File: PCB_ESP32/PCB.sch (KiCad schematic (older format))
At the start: 26 parts, among them J3 I2C, J4 I2C, J5 WindVane, J6 WindSpeed, J7 ATTINY24, J7 Rain, J8 ReedSwitches-WindVane, U1 MCP1702-5002E_TO92 5V, U2 MCP1700-3302E_TO92 3.3V, U5 ATtiny24A-PU WindDir

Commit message: PCB for ESP32
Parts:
- removed C12: 100nF, symbol Device:C_Small
- removed J7: ATTINY24, symbol Connector_Generic:Conn_01x04
- removed J8: ReedSwitches-WindVane, symbol Connector_Generic:Conn_02x05_Odd_Even
- removed U5: ATtiny24A-PU WindDir, Package_DIP:DIP-14_W7.62mm, symbol MCU_Microchip_ATtiny:ATtiny24A-PU
- added C8, C9: 0.1uF, Capacitor_THT:CP_Radial_Tantal_D4.5mm_P5.00mm, symbol Device:C
- added R5: 20M, Resistor_THT:R_Axial_DIN0207_L6.3mm_D2.5mm_P10.16mm_Horizontal, symbol Device:R
- added R6, R8: 10M, Resistor_THT:R_Axial_DIN0207_L6.3mm_D2.5mm_P10.16mm_Horizontal, symbol Device:R
- added R7: 5M2, Resistor_THT:R_Axial_DIN0207_L6.3mm_D2.5mm_P10.16mm_Horizontal, symbol Device:R
- C1: footprint (none) -> Capacitor_THT:CP_Radial_D8.0mm_P5.00mm
- C2: renamed from C10; footprint (none) -> Capacitor_THT:CP_Radial_Tantal_D4.5mm_P5.00mm
- C3: renamed from C9; footprint (none) -> Capacitor_THT:CP_Radial_Tantal_D4.5mm_P5.00mm
- C4: renamed from C2; footprint (none) -> Capacitor_THT:CP_Radial_D8.0mm_P5.00mm
- C5: renamed from C3; footprint (none) -> Capacitor_THT:CP_Radial_D8.0mm_P5.00mm
- C6: renamed from C7; footprint (none) -> Capacitor_THT:CP_Radial_Tantal_D4.5mm_P5.00mm
- C7: renamed from C8; footprint (none) -> Capacitor_THT:CP_Radial_Tantal_D4.5mm_P5.00mm
- D1: footprint (none) -> Diode_THT:D_DO-41_SOD81_P10.16mm_Horizontal
- GND1, GND2: footprint (none) -> Connector_JST:JST_XH_B2B-XH-AM_1x02_P2.50mm_Vertical
- J3, J4: footprint (none) -> Connector_JST:JST_XH_B4B-XH-A_1x04_P2.50mm_Vertical
- J5: footprint (none) -> Connector_PinHeader_2.54mm:PinHeader_2x05_P2.54mm_Vertical
- J6, J7: footprint (none) -> Connector_JST:JST_XH_B3B-XH-A_1x03_P2.50mm_Vertical
- R1, R2, R3, R4: footprint (none) -> Resistor_THT:R_Axial_DIN0207_L6.3mm_D2.5mm_P10.16mm_Horizontal
- U3: renamed from U?; footprint RF_Module:ESP32-WROOM-32 -> PCB_ESP32:ESP32DevKit
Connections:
- net GND: now also C8.1, C9.1, R6.2, R8.2
- net at C1.1, C2.2, GND1.2 (Pin_2)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: now also R5.1
- net at U3.6 (IO34): now also C8.2, R5.2, R6.1
- net at U3.7 (IO35): now also C9.2, R7.2, R8.1

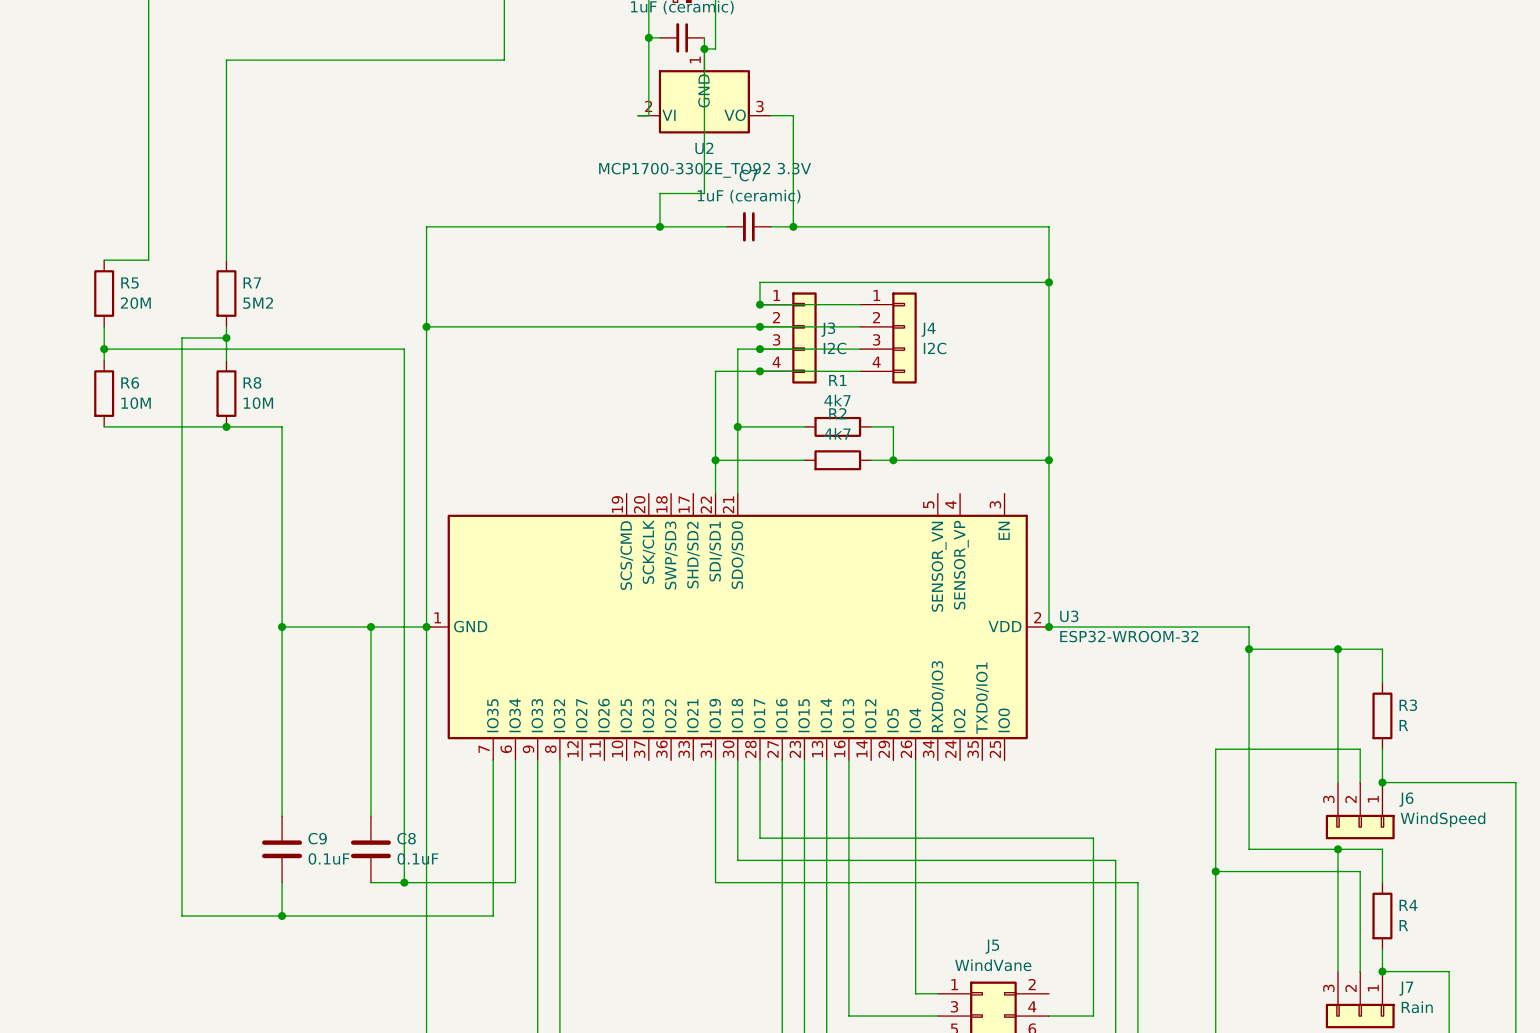
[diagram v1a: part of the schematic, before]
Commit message: ESP32 Code complete
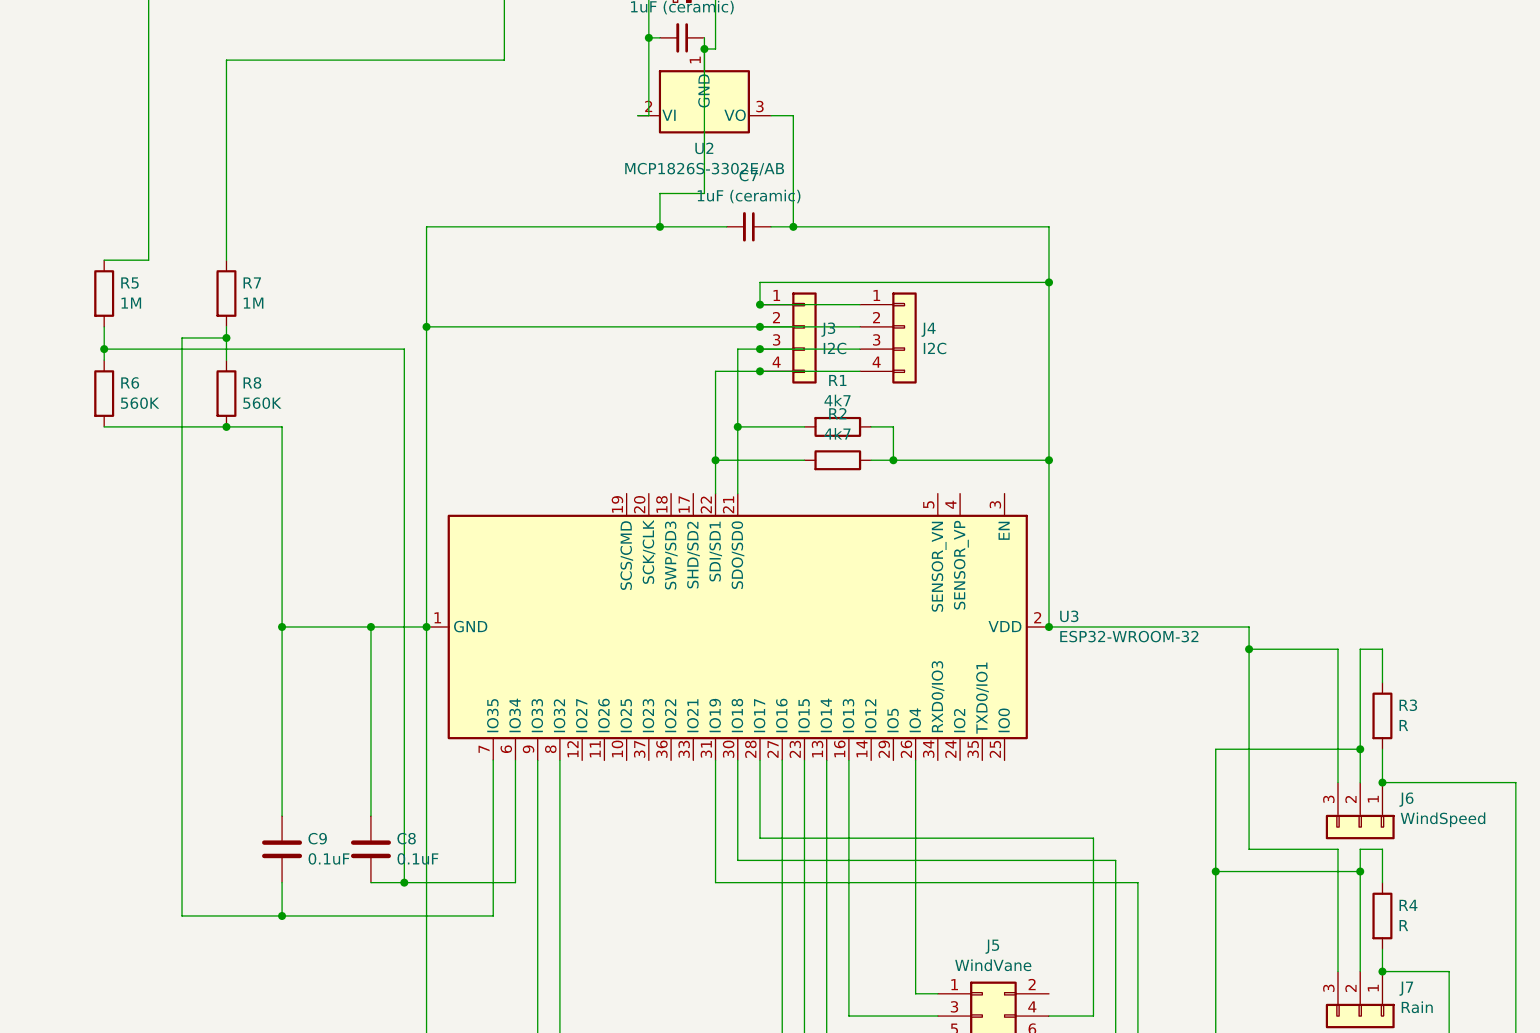
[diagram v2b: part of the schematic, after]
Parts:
- R5: value 20M -> 1M
- R6, R8: value 10M -> 560K
- R7: value 5M2 -> 1M
- U2: value MCP1700-3302E_TO92 3.3V -> MCP1826S-3302E/AB
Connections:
- net GND: now also R3.1, R4.1
- net at C7.1, J3.1 (Pin_1), J4.1 (Pin_1)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: no longer R3.1, R4.1
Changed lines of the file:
@@
 EESchema Schematic File Version 4
 LIBS:PCB-cache
-EELAYER 30 0
+EELAYER 29 0
 EELAYER END
 $Descr A4 11693 8268
@@
 P 3600 2050
 F 0 "U2" H 3600 1901 50  0000 C CNN
-F 1 "MCP1700-3302E_TO92 3.3V" H 3600 1810 50  0000 C CNN
+F 1 "MCP1826S-3302E/AB" H 3600 1810 50  0000 C CNN
 F 2 "Package_TO_SOT_THT:TO-92_Inline" H 3600 1850 50  0001 C CIN
 F 3 "http://ww1.microchip.com/downloads/en/DeviceDoc/20001826D.pdf" H 3600 2050 50  0001 C CNN
@@
 $EndComp
 Wire Wire Line
-	6450 5350 6650 5350
-Wire Wire Line
 	6650 5350 6650 5500
-Connection ~ 6450 5350
 Wire Wire Line
 	6650 5900 6650 5800
@@
 Wire Wire Line
 	6650 4600 6650 4450
-Wire Wire Line
-	6650 4450 6450 4450
-Connection ~ 6450 4450
 Wire Wire Line
 	6650 5900 6950 5900
@@
 P 900 2850
 F 0 "R5" H 970 2896 50  0000 L CNN
-F 1 "20M" H 970 2805 50  0000 L CNN
+F 1 "1M" H 970 2805 50  0000 L CNN
 F 2 "Resistor_THT:R_Axial_DIN0207_L6.3mm_D2.5mm_P10.16mm_Horizontal" V 830 2850 50  0001 C CNN
 F 3 "~" H 900 2850 50  0001 C CNN
@@
 P 900 3300
 F 0 "R6" H 970 3346 50  0000 L CNN
-F 1 "10M" H 970 3255 50  0000 L CNN
+F 1 "560K" H 970 3255 50  0000 L CNN
 F 2 "Resistor_THT:R_Axial_DIN0207_L6.3mm_D2.5mm_P10.16mm_Horizontal" V 830 3300 50  0001 C CNN
 F 3 "~" H 900 3300 50  0001 C CNN
@@
 P 1450 2850
 F 0 "R7" H 1520 2896 50  0000 L CNN
-F 1 "5M2" H 1520 2805 50  0000 L CNN
+F 1 "1M" H 1520 2805 50  0000 L CNN
 F 2 "Resistor_THT:R_Axial_DIN0207_L6.3mm_D2.5mm_P10.16mm_Horizontal" V 1380 2850 50  0001 C CNN
 F 3 "~" H 1450 2850 50  0001 C CNN
@@
 P 1450 3300
 F 0 "R8" H 1520 3346 50  0000 L CNN
-F 1 "10M" H 1520 3255 50  0000 L CNN
+F 1 "560K" H 1520 3255 50  0000 L CNN
 F 2 "Resistor_THT:R_Axial_DIN0207_L6.3mm_D2.5mm_P10.16mm_Horizontal" V 1380 3300 50  0001 C CNN
 F 3 "~" H 1450 3300 50  0001 C CNN
@@
 Wire Wire Line
 	1450 1800 1450 2700
+Wire Wire Line
+	6550 4900 6550 4450
+Wire Wire Line
+	6550 4450 6650 4450
+Connection ~ 6550 4900
+Wire Wire Line
+	6550 5450 6550 5350
+Wire Wire Line
+	6550 5350 6650 5350
+Connection ~ 6550 5450
 $EndSCHEMATC
